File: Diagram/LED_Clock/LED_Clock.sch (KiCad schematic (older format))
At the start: 11 parts, among them SW1 SW_Push_Dual, U1 ATmega328P-PU, U2 DS3231MZ, U5 Barreljack, U6 JST4pin, Y1 Crystal

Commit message: updated
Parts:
- U5: symbol Personal:Barreljack -> LED_Clock-rescue:Barreljack-Personal
- U6: symbol Personal:JST4pin -> LED_Clock-rescue:JST4pin-Personal
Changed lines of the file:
@@
 $EndComp
 $Comp
-L Personal:Barreljack U5
+L LED_Clock-rescue:Barreljack-Personal U5
 U 1 1 5E90BB97
 P 5150 7450
@@
 $EndComp
 $Comp
-L Personal:JST4pin U6
+L LED_Clock-rescue:JST4pin-Personal U6
 U 1 1 5E96772E
 P 6100 4450

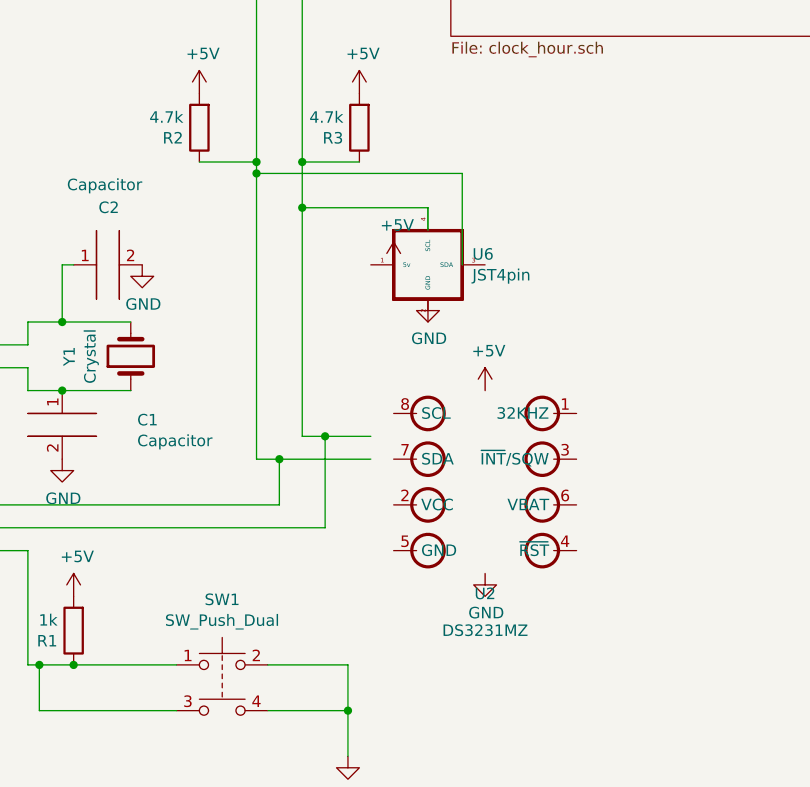
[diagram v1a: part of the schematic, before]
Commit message: Updated
led flipped the RTS symbol remade and JST4pin enlarged
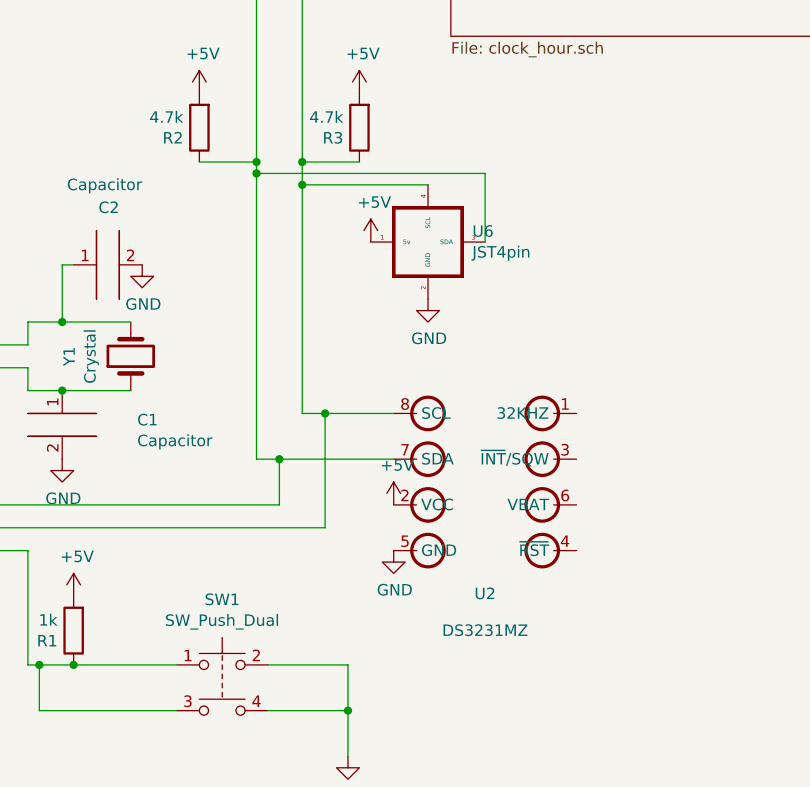
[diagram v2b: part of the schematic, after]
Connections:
- wire segments 49 -> 48
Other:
- moved on the sheet: U6
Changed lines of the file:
@@
 L power:+5V #PWR011
 U 1 1 5E731C95
-P 6350 5000
-F 0 "#PWR011" H 6350 4850 50  0001 C CNN
-F 1 "+5V" H 6365 5173 50  0000 C CNN
-F 2 "" H 6350 5000 50  0001 C CNN
-F 3 "" H 6350 5000 50  0001 C CNN
-	1    6350 5000
+P 5950 5500
+F 0 "#PWR011" H 5950 5350 50  0001 C CNN
+F 1 "+5V" H 5965 5673 50  0000 C CNN
+F 2 "" H 5950 5500 50  0001 C CNN
+F 3 "" H 5950 5500 50  0001 C CNN
+	1    5950 5500
 	1    0    0    -1
 $EndComp
@@
 L power:GND #PWR012
 U 1 1 5E731CA7
-P 6350 5800
-F 0 "#PWR012" H 6350 5550 50  0001 C CNN
-F 1 "GND" H 6355 5627 50  0000 C CNN
-F 2 "" H 6350 5800 50  0001 C CNN
-F 3 "" H 6350 5800 50  0001 C CNN
-	1    6350 5800
+P 5950 5700
+F 0 "#PWR012" H 5950 5450 50  0001 C CNN
+F 1 "GND" H 5955 5527 50  0000 C CNN
+F 2 "" H 5950 5700 50  0001 C CNN
+F 3 "" H 5950 5700 50  0001 C CNN
+	1    5950 5700
 	1    0    0    -1
 $EndComp
@@
 Wire Wire Line
 	4500 2750 3800 2750
-Wire Wire Line
-	5850 5200 5650 5200
-Wire Wire Line
-	5550 5200 5550 4200
 Connection ~ 5550 2600
 Wire Wire Line
 	5550 2600 4500 2600
-Wire Wire Line
-	5850 5300 5450 5300
-Wire Wire Line
-	5350 5300 5350 4050
 Connection ~ 5350 2350
 Wire Wire Line
@@
 Wire Wire Line
 	3950 5600 5650 5600
-Wire Wire Line
-	5650 5600 5650 5200
-Connection ~ 5650 5200
-Wire Wire Line
-	5650 5200 5550 5200
 $Comp
 L Device:R R?
@@
 $EndComp
 $Comp
-L LED_Clock-rescue:JST4pin-Personal U6
-U 1 1 5E96772E
-P 6100 4450
-F 0 "U6" H 6294 4496 50  0000 L CNN
-F 1 "JST4pin" H 6294 4405 50  0000 L CNN
-F 2 "Connector_JST:JST_SH_SM04B-SRSS-TB_1x04-1MP_P1.00mm_Horizontal" H 6100 4450 50  0001 C CNN
-F 3 "" H 6100 4450 50  0001 C CNN
-	1    6100 4450
-	1    0    0    -1
-$EndComp
-$Comp
 L power:+5V #PWR0106
 U 1 1 5E9693AB
-P 5950 4450
-F 0 "#PWR0106" H 5950 4300 50  0001 C CNN
-F 1 "+5V" H 5965 4623 50  0000 C CNN
-F 2 "" H 5950 4450 50  0001 C CNN
-F 3 "" H 5950 4450 50  0001 C CNN
-	1    5950 4450
+P 5850 4350
+F 0 "#PWR0106" H 5850 4200 50  0001 C CNN
+F 1 "+5V" H 5865 4523 50  0000 C CNN
+F 2 "" H 5850 4350 50  0001 C CNN
+F 3 "" H 5850 4350 50  0001 C CNN
+	1    5850 4350
 	1    0    0    -1
 $EndComp
@@
 	1    0    0    -1
 $EndComp
-Wire Wire Line
-	5550 4200 6100 4200
-Wire Wire Line
-	6100 4200 6100 4300
-Connection ~ 5550 4200
-Wire Wire Line
-	5550 4200 5550 4000
-Wire Wire Line
-	5350 4050 6250 4050
-Wire Wire Line
-	6250 4050 6250 4450
+$Comp
+L LED_Clock-rescue:JST4pin-Personal U6
+U 1 1 5E96772E
+P 6100 4350
+F 0 "U6" H 6294 4396 50  0000 L CNN
+F 1 "JST4pin" H 6294 4305 50  0000 L CNN
+F 2 "Connector_JST:JST_SH_SM04B-SRSS-TB_1x04-1MP_P1.00mm_Horizontal" H 6100 4350 50  0001 C CNN
+F 3 "" H 6100 4350 50  0001 C CNN
+	1    6100 4350
+	1    0    0    -1
+$EndComp
+Wire Wire Line
+	5350 4000 5350 4050
+Wire Wire Line
+	5550 4000 5550 4100
+Wire Wire Line
+	5550 4100 6100 4100
+Wire Wire Line
+	5350 4050 6350 4050
+Wire Wire Line
+	6350 4050 6350 4350
 Connection ~ 5350 4050
 Wire Wire Line
-	5350 4050 5350 4000
+	5350 4050 5350 5300
+Wire Wire Line
+	5950 5100 5650 5100
+Wire Wire Line
+	5550 5100 5550 4100
+Connection ~ 5550 4100
+Wire Wire Line
+	5650 5100 5650 5600
+Connection ~ 5650 5100
+Wire Wire Line
+	5650 5100 5550 5100
+Wire Wire Line
+	5450 5300 5950 5300
 $EndSCHEMATC

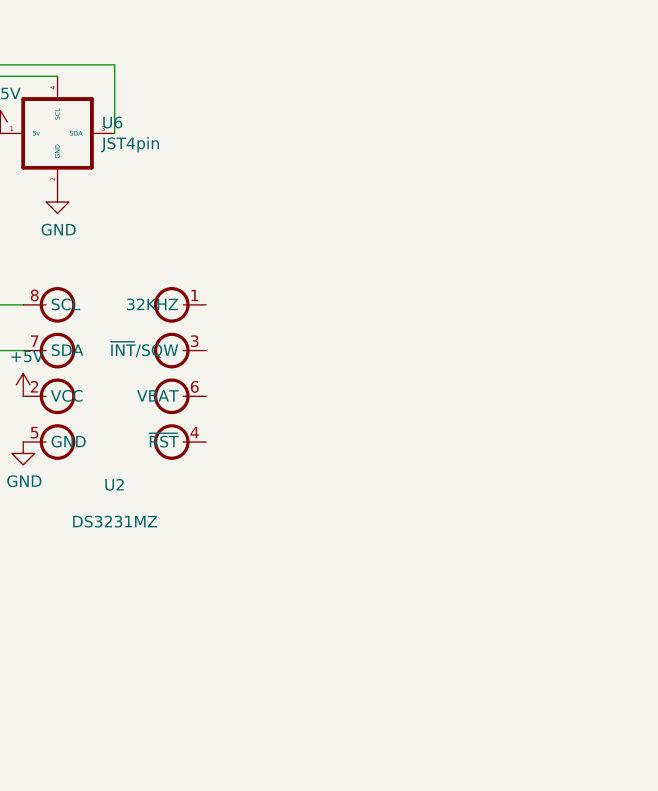
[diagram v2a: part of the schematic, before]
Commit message: update 1.2
new mounting holes jst4 pin mounting points to ground and refilled
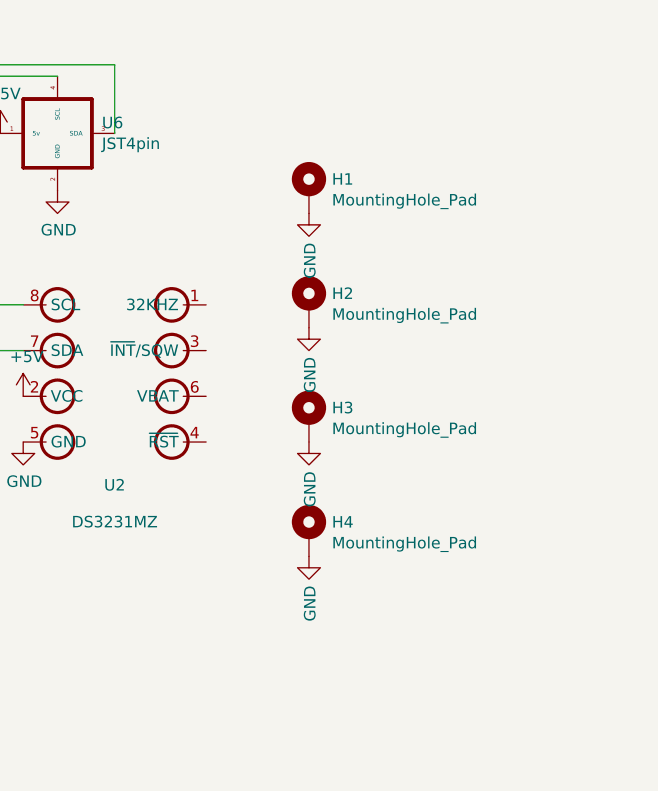
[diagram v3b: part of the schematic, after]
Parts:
- added H1, H2, H3, H4: MountingHole_Pad, MountingHole:MountingHole_3.5mm_Pad, symbol Mechanical:MountingHole_Pad
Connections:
- net GND: now also H1.1, H2.1, H3.1, H4.1
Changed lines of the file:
@@
 Wire Wire Line
 	5450 5300 5950 5300
+$Comp
+L Mechanical:MountingHole_Pad H2
+U 1 1 5E98A51C
+P 7200 5100
+F 0 "H2" H 7300 5149 50  0000 L CNN
+F 1 "MountingHole_Pad" H 7300 5058 50  0000 L CNN
+F 2 "MountingHole:MountingHole_3.5mm_Pad" H 7200 5100 50  0001 C CNN
+F 3 "~" H 7200 5100 50  0001 C CNN
+	1    7200 5100
+	1    0    0    -1
+$EndComp
+$Comp
+L Mechanical:MountingHole_Pad H1
+U 1 1 5E98BC5C
+P 7200 4600
+F 0 "H1" H 7300 4649 50  0000 L CNN
+F 1 "MountingHole_Pad" H 7300 4558 50  0000 L CNN
+F 2 "MountingHole:MountingHole_3.5mm_Pad" H 7200 4600 50  0001 C CNN
+F 3 "~" H 7200 4600 50  0001 C CNN
+	1    7200 4600
+	1    0    0    -1
+$EndComp
+$Comp
+L Mechanical:MountingHole_Pad H3
+U 1 1 5E98C298
+P 7200 5600
+F 0 "H3" H 7300 5649 50  0000 L CNN
+F 1 "MountingHole_Pad" H 7300 5558 50  0000 L CNN
+F 2 "MountingHole:MountingHole_3.5mm_Pad" H 7200 5600 50  0001 C CNN
+F 3 "~" H 7200 5600 50  0001 C CNN
+	1    7200 5600
+	1    0    0    -1
+$EndComp
+$Comp
+L Mechanical:MountingHole_Pad H4
+U 1 1 5E98CAE0
+P 7200 6100
+F 0 "H4" H 7300 6149 50  0000 L CNN
+F 1 "MountingHole_Pad" H 7300 6058 50  0000 L CNN
+F 2 "MountingHole:MountingHole_3.5mm_Pad" H 7200 6100 50  0001 C CNN
+F 3 "~" H 7200 6100 50  0001 C CNN
+	1    7200 6100
+	1    0    0    -1
+$EndComp
+$Comp
+L power:GND #PWR0108
+U 1 1 5E990D8F
+P 7200 4700
+F 0 "#PWR0108" H 7200 4450 50  0001 C CNN
+F 1 "GND" V 7205 4572 50  0000 R CNN
+F 2 "" H 7200 4700 50  0001 C CNN
+F 3 "" H 7200 4700 50  0001 C CNN
+	1    7200 4700
+	1    0    0    -1
+$EndComp
+$Comp
+L power:GND #PWR0109
+U 1 1 5E993FEE
+P 7200 5200
+F 0 "#PWR0109" H 7200 4950 50  0001 C CNN
+F 1 "GND" V 7205 5072 50  0000 R CNN
+F 2 "" H 7200 5200 50  0001 C CNN
+F 3 "" H 7200 5200 50  0001 C CNN
+	1    7200 5200
+	1    0    0    -1
+$EndComp
+$Comp
+L power:GND #PWR0110
+U 1 1 5E994521
+P 7200 6200
+F 0 "#PWR0110" H 7200 5950 50  0001 C CNN
+F 1 "GND" V 7205 6072 50  0000 R CNN
+F 2 "" H 7200 6200 50  0001 C CNN
+F 3 "" H 7200 6200 50  0001 C CNN
+	1    7200 6200
+	1    0    0    -1
+$EndComp
+$Comp
+L power:GND #PWR0111
+U 1 1 5E994871
+P 7200 5700
+F 0 "#PWR0111" H 7200 5450 50  0001 C CNN
+F 1 "GND" V 7205 5572 50  0000 R CNN
+F 2 "" H 7200 5700 50  0001 C CNN
+F 3 "" H 7200 5700 50  0001 C CNN
+	1    7200 5700
+	1    0    0    -1
+$EndComp
 $EndSCHEMATC
